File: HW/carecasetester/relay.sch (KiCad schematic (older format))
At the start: 1 part

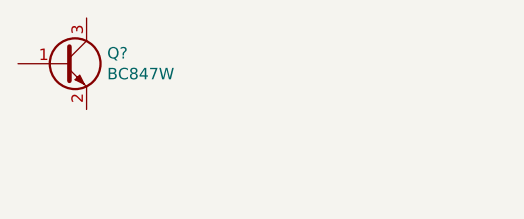
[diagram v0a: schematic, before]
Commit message: Main sheet saved still need to make relay sheet again
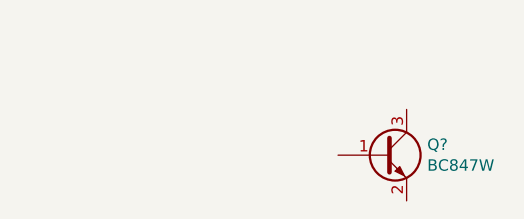
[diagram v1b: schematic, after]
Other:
- moved on the sheet: Q?
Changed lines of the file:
@@
 L Transistor_BJT:BC847W Q?
 U 1 1 5E853643
-P 3875 3400
-F 0 "Q?" H 4065 3446 50  0000 L CNN
-F 1 "BC847W" H 4065 3355 50  0000 L CNN
-F 2 "Package_TO_SOT_SMD:SOT-323_SC-70" H 4075 3325 50  0001 L CIN
-F 3 "http://www.infineon.com/dgdl/Infineon-BC847SERIES_BC848SERIES_BC849SERIES_BC850SERIES-DS-v01_01-en.pdf?fileId=db3a304314dca389011541d4630a1657" H 3875 3400 50  0001 L CNN
-	1    3875 3400
+P 5275 3800
+F 0 "Q?" H 5465 3846 50  0000 L CNN
+F 1 "BC847W" H 5465 3755 50  0000 L CNN
+F 2 "Package_TO_SOT_SMD:SOT-323_SC-70" H 5475 3725 50  0001 L CIN
+F 3 "http://www.infineon.com/dgdl/Infineon-BC847SERIES_BC848SERIES_BC849SERIES_BC850SERIES-DS-v01_01-en.pdf?fileId=db3a304314dca389011541d4630a1657" H 5275 3800 50  0001 L CNN
+	1    5275 3800
 	1    0    0    -1
 $EndComp

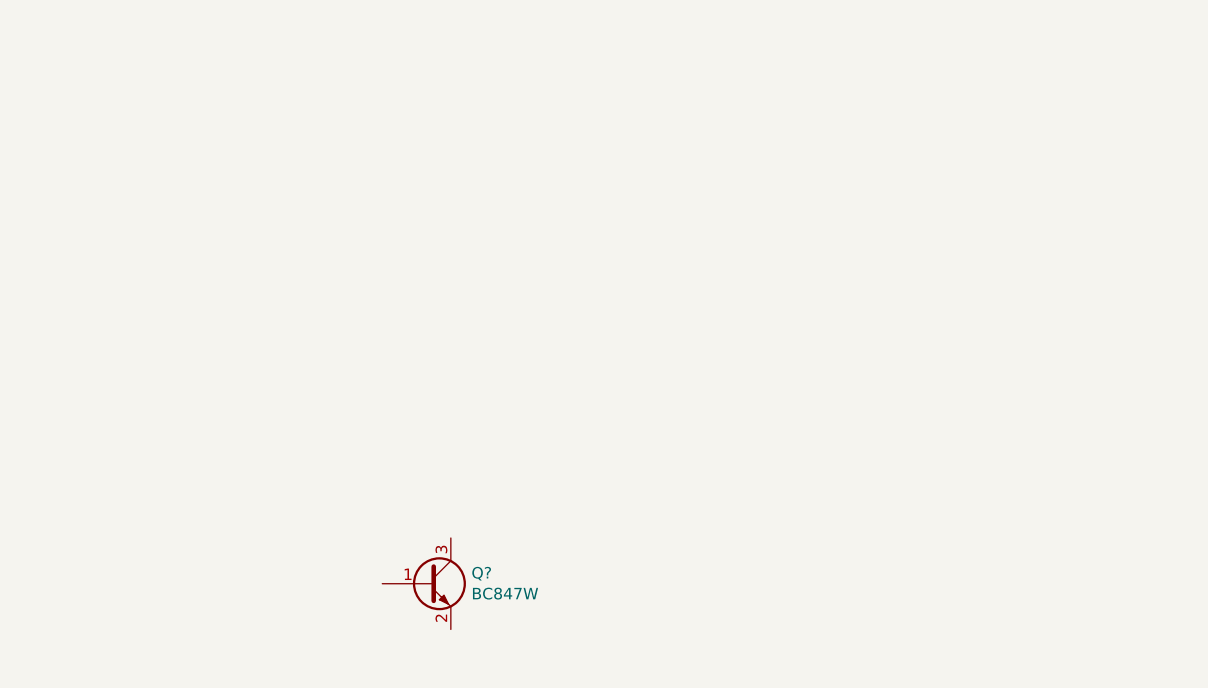
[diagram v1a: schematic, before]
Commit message: Relay sheet filled and all pins matched.
starting changes made to pcb to fit schematic to the new pcb
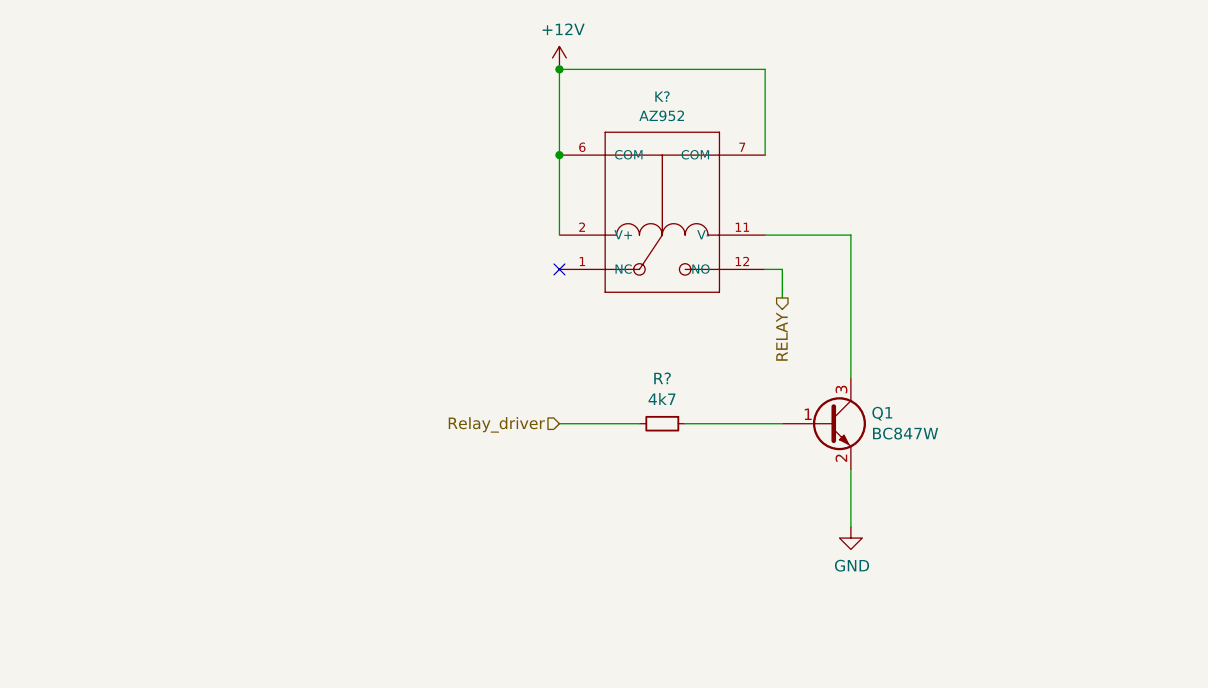
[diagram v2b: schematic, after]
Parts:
- added K?: AZ952, symbol athir:AZ952
- added R?: 4k7, symbol Device:R_Small
- gave numbers to parts that had none: 1
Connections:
- net at Q1.1 (B): now also R?.1
- net GND: now reaches Q1.2 (E)
- net at Q1.3 (C): now also K?.11 (V-)
- new net +12V: K?.2 (V+), K?.6 (COM), K?.7 (COM)
- new net RELAY: K?.12 (NO)
- new net Relay_driver: R?.2
- no-connect marks 0 -> 1
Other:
- moved on the sheet: Q1
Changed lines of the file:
@@
 $EndDescr
 $Comp
-L Transistor_BJT:BC847W Q?
+L Transistor_BJT:BC847W Q1
 U 1 1 5E853643
-P 5275 3800
-F 0 "Q?" H 5465 3846 50  0000 L CNN
-F 1 "BC847W" H 5465 3755 50  0000 L CNN
-F 2 "Package_TO_SOT_SMD:SOT-323_SC-70" H 5475 3725 50  0001 L CIN
-F 3 "http://www.infineon.com/dgdl/Infineon-BC847SERIES_BC848SERIES_BC849SERIES_BC850SERIES-DS-v01_01-en.pdf?fileId=db3a304314dca389011541d4630a1657" H 5275 3800 50  0001 L CNN
-	1    5275 3800
+P 7025 3100
+F 0 "Q1" H 7215 3146 50  0000 L CNN
+F 1 "BC847W" H 7215 3055 50  0000 L CNN
+F 2 "Package_TO_SOT_SMD:SOT-323_SC-70" H 7225 3025 50  0001 L CIN
+F 3 "http://www.infineon.com/dgdl/Infineon-BC847SERIES_BC848SERIES_BC849SERIES_BC850SERIES-DS-v01_01-en.pdf?fileId=db3a304314dca389011541d4630a1657" H 7025 3100 50  0001 L CNN
+	1    7025 3100
 	1    0    0    -1
 $EndComp
+$Comp
+L athir:AZ952 K?
+U 1 1 5E85B068
+P 6300 2175
+F 0 "K?" V 6804 2175 45  0000 C CNN
+F 1 "AZ952" V 6720 2175 45  0000 C CNN
+F 2 "" H 6300 2125 60  0001 C CNN
+F 3 "" H 6300 2125 60  0001 C CNN
+F 4 "315030000" H 6330 2275 20  0001 C CNN "SKU"
+	1    6300 2175
+	0    -1   -1   0
+$EndComp
+NoConn ~ 5850 2425
+Wire Wire Line
+	6750 1925 6750 1550
+Wire Wire Line
+	6750 1550 5850 1550
+Wire Wire Line
+	5850 1550 5850 1925
+Wire Wire Line
+	5850 2275 5850 1925
+Connection ~ 5850 1925
+$Comp
+L power:+12V #PWR?
+U 1 1 5E85C22D
+P 5850 1550
+F 0 "#PWR?" H 5850 1400 50  0001 C CNN
+F 1 "+12V" H 5865 1723 50  0000 C CNN
+F 2 "" H 5850 1550 50  0001 C CNN
+F 3 "" H 5850 1550 50  0001 C CNN
+	1    5850 1550
+	1    0    0    -1
+$EndComp
+Connection ~ 5850 1550
+Wire Wire Line
+	6750 2275 7125 2275
+Wire Wire Line
+	7125 2275 7125 2900
+$Comp
+L power:GND #PWR?
+U 1 1 5E85E92E
+P 7125 3550
+F 0 "#PWR?" H 7125 3300 50  0001 C CNN
+F 1 "GND" H 7130 3377 50  0000 C CNN
+F 2 "" H 7125 3550 50  0001 C CNN
+F 3 "" H 7125 3550 50  0001 C CNN
+	1    7125 3550
+	1    0    0    -1
+$EndComp
+Wire Wire Line
+	7125 3300 7125 3550
+$Comp
+L Device:R_Small R?
+U 1 1 5E85EFB5
+P 6300 3100
+F 0 "R?" V 6104 3100 50  0000 C CNN
+F 1 "4k7" V 6195 3100 50  0000 C CNN
+F 2 "" H 6300 3100 50  0001 C CNN
+F 3 "~" H 6300 3100 50  0001 C CNN
+	1    6300 3100
+	0    1    1    0
+$EndComp
+Wire Wire Line
+	6400 3100 6825 3100
+Text HLabel 5850 3100 0    50   Input ~ 0
+Relay_driver
+Wire Wire Line
+	5850 3100 6200 3100
+Text HLabel 6825 2550 3    50   Output ~ 0
+RELAY
+Wire Wire Line
+	6750 2425 6825 2425
+Wire Wire Line
+	6825 2425 6825 2550
 $EndSCHEMATC

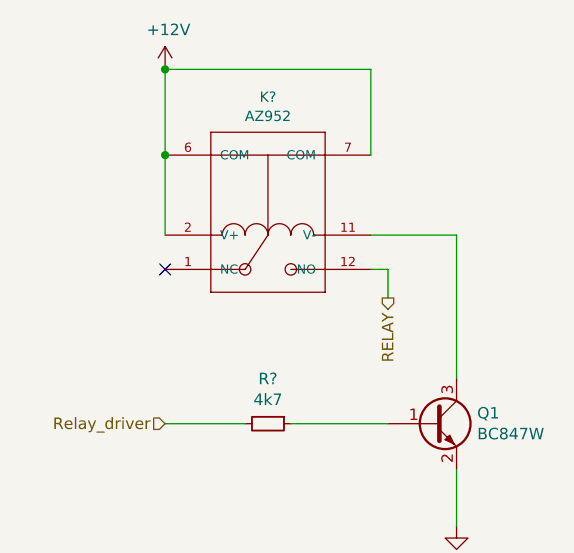
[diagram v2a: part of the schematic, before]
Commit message: First try to fit schematic to pcb (not imported footprints to pcb yet)
Schematic: All known components has gotten an updated footprint
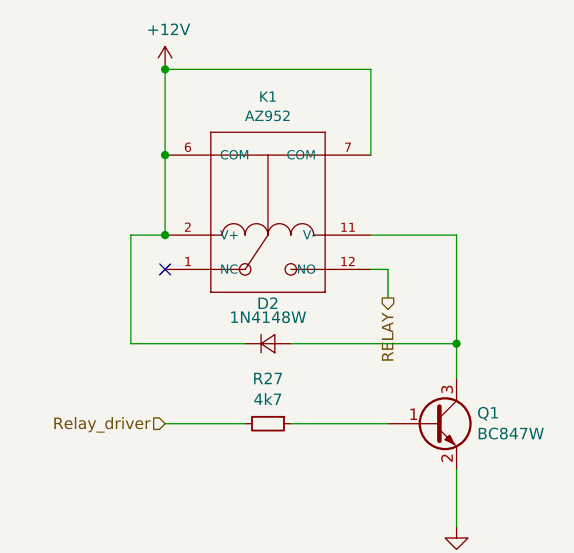
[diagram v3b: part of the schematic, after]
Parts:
- added D2: 1N4148W, Diode_THT:D_DO-35_SOD27_P10.16mm_Horizontal, symbol Device:D_Small
- K1: renamed from K?; footprint (none) -> athir:AZ952
- R27: renamed from R?; footprint (none) -> Resistor_SMD:R_0603_1608Metric_Pad1.05x0.95mm_HandSolder
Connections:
- net +12V: now also D2.1 (K)
- net at K1.11 (V-), Q1.3 (C): now also D2.2 (A)
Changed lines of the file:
@@
 $EndComp
 $Comp
-L athir:AZ952 K?
+L athir:AZ952 K1
 U 1 1 5E85B068
 P 6300 2175
-F 0 "K?" V 6804 2175 45  0000 C CNN
+F 0 "K1" V 6804 2175 45  0000 C CNN
 F 1 "AZ952" V 6720 2175 45  0000 C CNN
-F 2 "" H 6300 2125 60  0001 C CNN
+F 2 "athir:AZ952" H 6300 2125 60  0001 C CNN
 F 3 "" H 6300 2125 60  0001 C CNN
 F 4 "315030000" H 6330 2275 20  0001 C CNN "SKU"
@@
 Connection ~ 5850 1925
 $Comp
-L power:+12V #PWR?
+L power:+12V #PWR01
 U 1 1 5E85C22D
 P 5850 1550
-F 0 "#PWR?" H 5850 1400 50  0001 C CNN
+F 0 "#PWR01" H 5850 1400 50  0001 C CNN
 F 1 "+12V" H 5865 1723 50  0000 C CNN
 F 2 "" H 5850 1550 50  0001 C CNN
@@
 	6750 2275 7125 2275
 Wire Wire Line
-	7125 2275 7125 2900
+	7125 2275 7125 2750
 $Comp
-L power:GND #PWR?
+L power:GND #PWR06
 U 1 1 5E85E92E
 P 7125 3550
-F 0 "#PWR?" H 7125 3300 50  0001 C CNN
+F 0 "#PWR06" H 7125 3300 50  0001 C CNN
 F 1 "GND" H 7130 3377 50  0000 C CNN
 F 2 "" H 7125 3550 50  0001 C CNN
@@
 	7125 3300 7125 3550
 $Comp
-L Device:R_Small R?
+L Device:R_Small R27
 U 1 1 5E85EFB5
 P 6300 3100
-F 0 "R?" V 6104 3100 50  0000 C CNN
+F 0 "R27" V 6104 3100 50  0000 C CNN
 F 1 "4k7" V 6195 3100 50  0000 C CNN
-F 2 "" H 6300 3100 50  0001 C CNN
+F 2 "Resistor_SMD:R_0603_1608Metric_Pad1.05x0.95mm_HandSolder" H 6300 3100 50  0001 C CNN
 F 3 "~" H 6300 3100 50  0001 C CNN
 	1    6300 3100
@@
 Wire Wire Line
 	6825 2425 6825 2550
+$Comp
+L Device:D_Small D2
+U 1 1 5E867CA9
+P 6300 2750
+F 0 "D2" H 6300 2925 50  0000 C CNN
+F 1 "1N4148W" H 6300 2864 50  0000 C CNN
+F 2 "Diode_THT:D_DO-35_SOD27_P10.16mm_Horizontal" V 6300 2750 50  0001 C CNN
+F 3 "~" V 6300 2750 50  0001 C CNN
+	1    6300 2750
+	1    0    0    -1
+$EndComp
+Wire Wire Line
+	6200 2750 5700 2750
+Wire Wire Line
+	5700 2750 5700 2275
+Wire Wire Line
+	5700 2275 5850 2275
+Connection ~ 5850 2275
+Wire Wire Line
+	6400 2750 7125 2750
+Connection ~ 7125 2750
+Wire Wire Line
+	7125 2750 7125 2900
 $EndSCHEMATC

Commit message: PCB and Schematic are synced and gerbers can be made
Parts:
- Q1: footprint Package_TO_SOT_SMD:SOT-323_SC-70 -> Package_TO_SOT_SMD:SOT-23
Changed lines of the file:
@@
 F 0 "Q1" H 7215 3146 50  0000 L CNN
 F 1 "BC847W" H 7215 3055 50  0000 L CNN
-F 2 "Package_TO_SOT_SMD:SOT-323_SC-70" H 7225 3025 50  0001 L CIN
+F 2 "Package_TO_SOT_SMD:SOT-23" H 7225 3025 50  0001 L CIN
 F 3 "http://www.infineon.com/dgdl/Infineon-BC847SERIES_BC848SERIES_BC849SERIES_BC850SERIES-DS-v01_01-en.pdf?fileId=db3a304314dca389011541d4630a1657" H 7025 3100 50  0001 L CNN
 	1    7025 3100

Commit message: V0.22 gerbers
2nd relay added and all should now be ready to order
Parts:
- added D3: 1N4148W, Diode_THT:D_DO-35_SOD27_P10.16mm_Horizontal, symbol Device:D_Small
- added K2: AZ952, athir:AZ952, symbol carecasetester-rescue:AZ952-athir
- added Q2: BC847W, Package_TO_SOT_SMD:SOT-23, symbol Transistor_BJT:BC847W
- added R29: 4k7, Resistor_SMD:R_0603_1608Metric_Pad1.05x0.95mm_HandSolder, symbol Device:R_Small
- K1: symbol athir:AZ952 -> carecasetester-rescue:AZ952-athir
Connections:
- net GND: now also Q2.2 (E)
- net RELAY renamed RELAY12V
- net Relay_driver renamed Relay_driver1
- new net: Q2.1 (B), R29.1
- new net: D3.2 (A), K2.11 (V-), Q2.3 (C)
- new net +5V: D3.1 (K), K2.2 (V+), K2.6 (COM), K2.7 (COM)
- new net RELAYBAT: K2.12 (NO)
- new net Relay_driver2: R29.2
- no-connect marks 1 -> 2
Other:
- moved on the sheet: D2, K1, Q1, R27
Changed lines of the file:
@@
 L Transistor_BJT:BC847W Q1
 U 1 1 5E853643
-P 7025 3100
-F 0 "Q1" H 7215 3146 50  0000 L CNN
-F 1 "BC847W" H 7215 3055 50  0000 L CNN
-F 2 "Package_TO_SOT_SMD:SOT-23" H 7225 3025 50  0001 L CIN
-F 3 "http://www.infineon.com/dgdl/Infineon-BC847SERIES_BC848SERIES_BC849SERIES_BC850SERIES-DS-v01_01-en.pdf?fileId=db3a304314dca389011541d4630a1657" H 7025 3100 50  0001 L CNN
-	1    7025 3100
-	1    0    0    -1
-$EndComp
-$Comp
-L athir:AZ952 K1
+P 5350 3475
+F 0 "Q1" H 5540 3521 50  0000 L CNN
+F 1 "BC847W" H 5540 3430 50  0000 L CNN
+F 2 "Package_TO_SOT_SMD:SOT-23" H 5550 3400 50  0001 L CIN
+F 3 "http://www.infineon.com/dgdl/Infineon-BC847SERIES_BC848SERIES_BC849SERIES_BC850SERIES-DS-v01_01-en.pdf?fileId=db3a304314dca389011541d4630a1657" H 5350 3475 50  0001 L CNN
+	1    5350 3475
+	1    0    0    -1
+$EndComp
+$Comp
+L carecasetester-rescue:AZ952-athir K1
 U 1 1 5E85B068
-P 6300 2175
-F 0 "K1" V 6804 2175 45  0000 C CNN
-F 1 "AZ952" V 6720 2175 45  0000 C CNN
-F 2 "athir:AZ952" H 6300 2125 60  0001 C CNN
-F 3 "" H 6300 2125 60  0001 C CNN
-F 4 "315030000" H 6330 2275 20  0001 C CNN "SKU"
-	1    6300 2175
+P 4625 2550
+AR Path="/5E85B068" Ref="K1"  Part="1"
+AR Path="/5E3E43C1/5E85B068" Ref="K1"  Part="1"
+F 0 "K1" V 5129 2550 45  0000 C CNN
+F 1 "AZ952" V 5045 2550 45  0000 C CNN
+F 2 "athir:AZ952" H 4625 2500 60  0001 C CNN
+F 3 "" H 4625 2500 60  0001 C CNN
+F 4 "315030000" H 4655 2650 20  0001 C CNN "SKU"
+	1    4625 2550
 	0    -1   -1   0
 $EndComp
-NoConn ~ 5850 2425
-Wire Wire Line
-	6750 1925 6750 1550
-Wire Wire Line
-	6750 1550 5850 1550
-Wire Wire Line
-	5850 1550 5850 1925
-Wire Wire Line
-	5850 2275 5850 1925
-Connection ~ 5850 1925
+NoConn ~ 4175 2800
+Wire Wire Line
+	5075 2300 5075 1925
+Wire Wire Line
+	5075 1925 4175 1925
+Wire Wire Line
+	4175 1925 4175 2300
+Wire Wire Line
+	4175 2650 4175 2300
+Connection ~ 4175 2300
 $Comp
 L power:+12V #PWR01
 U 1 1 5E85C22D
-P 5850 1550
-F 0 "#PWR01" H 5850 1400 50  0001 C CNN
-F 1 "+12V" H 5865 1723 50  0000 C CNN
-F 2 "" H 5850 1550 50  0001 C CNN
-F 3 "" H 5850 1550 50  0001 C CNN
-	1    5850 1550
-	1    0    0    -1
-$EndComp
-Connection ~ 5850 1550
-Wire Wire Line
-	6750 2275 7125 2275
-Wire Wire Line
-	7125 2275 7125 2750
+P 4175 1925
+F 0 "#PWR01" H 4175 1775 50  0001 C CNN
+F 1 "+12V" H 4190 2098 50  0000 C CNN
+F 2 "" H 4175 1925 50  0001 C CNN
+F 3 "" H 4175 1925 50  0001 C CNN
+	1    4175 1925
+	1    0    0    -1
+$EndComp
+Connection ~ 4175 1925
+Wire Wire Line
+	5075 2650 5450 2650
+Wire Wire Line
+	5450 2650 5450 3125
 $Comp
 L power:GND #PWR06
 U 1 1 5E85E92E
-P 7125 3550
-F 0 "#PWR06" H 7125 3300 50  0001 C CNN
-F 1 "GND" H 7130 3377 50  0000 C CNN
-F 2 "" H 7125 3550 50  0001 C CNN
-F 3 "" H 7125 3550 50  0001 C CNN
-	1    7125 3550
-	1    0    0    -1
-$EndComp
-Wire Wire Line
-	7125 3300 7125 3550
+P 5450 3925
+F 0 "#PWR06" H 5450 3675 50  0001 C CNN
+F 1 "GND" H 5455 3752 50  0000 C CNN
+F 2 "" H 5450 3925 50  0001 C CNN
+F 3 "" H 5450 3925 50  0001 C CNN
+	1    5450 3925
+	1    0    0    -1
+$EndComp
+Wire Wire Line
+	5450 3675 5450 3925
 $Comp
 L Device:R_Small R27
 U 1 1 5E85EFB5
-P 6300 3100
-F 0 "R27" V 6104 3100 50  0000 C CNN
-F 1 "4k7" V 6195 3100 50  0000 C CNN
-F 2 "Resistor_SMD:R_0603_1608Metric_Pad1.05x0.95mm_HandSolder" H 6300 3100 50  0001 C CNN
-F 3 "~" H 6300 3100 50  0001 C CNN
-	1    6300 3100
+P 4625 3475
+F 0 "R27" V 4429 3475 50  0000 C CNN
+F 1 "4k7" V 4520 3475 50  0000 C CNN
+F 2 "Resistor_SMD:R_0603_1608Metric_Pad1.05x0.95mm_HandSolder" H 4625 3475 50  0001 C CNN
+F 3 "~" H 4625 3475 50  0001 C CNN
+	1    4625 3475
 	0    1    1    0
 $EndComp
 Wire Wire Line
-	6400 3100 6825 3100
-Text HLabel 5850 3100 0    50   Input ~ 0
-Relay_driver
-Wire Wire Line
-	5850 3100 6200 3100
-Text HLabel 6825 2550 3    50   Output ~ 0
-RELAY
-Wire Wire Line
-	6750 2425 6825 2425
-Wire Wire Line
-	6825 2425 6825 2550
+	4725 3475 5150 3475
+Text HLabel 4175 3475 0    50   Input ~ 0
+Relay_driver1
+Wire Wire Line
+	4175 3475 4525 3475
+Text HLabel 5150 2925 3    50   Output ~ 0
+RELAY12V
+Wire Wire Line
+	5075 2800 5150 2800
+Wire Wire Line
+	5150 2800 5150 2925
 $Comp
 L Device:D_Small D2
 U 1 1 5E867CA9
-P 6300 2750
-F 0 "D2" H 6300 2925 50  0000 C CNN
-F 1 "1N4148W" H 6300 2864 50  0000 C CNN
-F 2 "Diode_THT:D_DO-35_SOD27_P10.16mm_Horizontal" V 6300 2750 50  0001 C CNN
-F 3 "~" V 6300 2750 50  0001 C CNN
-	1    6300 2750
-	1    0    0    -1
-$EndComp
-Wire Wire Line
-	6200 2750 5700 2750
-Wire Wire Line
-	5700 2750 5700 2275
-Wire Wire Line
-	5700 2275 5850 2275
-Connection ~ 5850 2275
-Wire Wire Line
-	6400 2750 7125 2750
-Connection ~ 7125 2750
-Wire Wire Line
-	7125 2750 7125 2900
+P 4625 3125
+F 0 "D2" H 4625 3300 50  0000 C CNN
+F 1 "1N4148W" H 4625 3239 50  0000 C CNN
+F 2 "Diode_THT:D_DO-35_SOD27_P10.16mm_Horizontal" V 4625 3125 50  0001 C CNN
+F 3 "~" V 4625 3125 50  0001 C CNN
+	1    4625 3125
+	1    0    0    -1
+$EndComp
+Wire Wire Line
+	4525 3125 4025 3125
+Wire Wire Line
+	4025 3125 4025 2650
+Wire Wire Line
+	4025 2650 4175 2650
+Connection ~ 4175 2650
+Wire Wire Line
+	4725 3125 5450 3125
+Connection ~ 5450 3125
+Wire Wire Line
+	5450 3125 5450 3275
+$Comp
+L Transistor_BJT:BC847W Q2
+U 1 1 5E8BC0FC
+P 8075 3500
+F 0 "Q2" H 8265 3546 50  0000 L CNN
+F 1 "BC847W" H 8265 3455 50  0000 L CNN
+F 2 "Package_TO_SOT_SMD:SOT-23" H 8275 3425 50  0001 L CIN
+F 3 "http://www.infineon.com/dgdl/Infineon-BC847SERIES_BC848SERIES_BC849SERIES_BC850SERIES-DS-v01_01-en.pdf?fileId=db3a304314dca389011541d4630a1657" H 8075 3500 50  0001 L CNN
+	1    8075 3500
+	1    0    0    -1
+$EndComp
+$Comp
+L carecasetester-rescue:AZ952-athir K?
+U 1 1 5E8BC103
+P 7350 2575
+AR Path="/5E8BC103" Ref="K?"  Part="1"
+AR Path="/5E3E43C1/5E8BC103" Ref="K2"  Part="1"
+F 0 "K2" V 7854 2575 45  0000 C CNN
+F 1 "AZ952" V 7770 2575 45  0000 C CNN
+F 2 "athir:AZ952" H 7350 2525 60  0001 C CNN
+F 3 "" H 7350 2525 60  0001 C CNN
+F 4 "315030000" H 7380 2675 20  0001 C CNN "SKU"
+	1    7350 2575
+	0    -1   -1   0
+$EndComp
+NoConn ~ 6900 2825
+Wire Wire Line
+	7800 2325 7800 1950
+Wire Wire Line
+	7800 1950 6900 1950
+Wire Wire Line
+	6900 1950 6900 2325
+Wire Wire Line
+	6900 2675 6900 2325
+Connection ~ 6900 2325
+Wire Wire Line
+	7800 2675 8175 2675
+Wire Wire Line
+	8175 2675 8175 3150
+$Comp
+L power:GND #PWR09
+U 1 1 5E8BC118
+P 8175 3950
+F 0 "#PWR09" H 8175 3700 50  0001 C CNN
+F 1 "GND" H 8180 3777 50  0000 C CNN
+F 2 "" H 8175 3950 50  0001 C CNN
+F 3 "" H 8175 3950 50  0001 C CNN
+	1    8175 3950
+	1    0    0    -1
+$EndComp
+Wire Wire Line
+	8175 3700 8175 3950
+$Comp
+L Device:R_Small R29
+U 1 1 5E8BC11F
+P 7350 3500
+F 0 "R29" V 7154 3500 50  0000 C CNN
+F 1 "4k7" V 7245 3500 50  0000 C CNN
+F 2 "Resistor_SMD:R_0603_1608Metric_Pad1.05x0.95mm_HandSolder" H 7350 3500 50  0001 C CNN
+F 3 "~" H 7350 3500 50  0001 C CNN
+	1    7350 3500
+	0    1    1    0
+$EndComp
+Wire Wire Line
+	7450 3500 7875 3500
+Text HLabel 6900 3500 0    50   Input ~ 0
+Relay_driver2
+Wire Wire Line
+	6900 3500 7250 3500
+Text HLabel 7875 2950 3    50   Output ~ 0
+RELAYBAT
+Wire Wire Line
+	7800 2825 7875 2825
+Wire Wire Line
+	7875 2825 7875 2950
+$Comp
+L Device:D_Small D3
+U 1 1 5E8BC12B
+P 7350 3150
+F 0 "D3" H 7350 3325 50  0000 C CNN
+F 1 "1N4148W" H 7350 3264 50  0000 C CNN
+F 2 "Diode_THT:D_DO-35_SOD27_P10.16mm_Horizontal" V 7350 3150 50  0001 C CNN
+F 3 "~" V 7350 3150 50  0001 C CNN
+	1    7350 3150
+	1    0    0    -1
+$EndComp
+Wire Wire Line
+	7250 3150 6750 3150
+Wire Wire Line
+	6750 3150 6750 2675
+Wire Wire Line
+	6750 2675 6900 2675
+Connection ~ 6900 2675
+Wire Wire Line
+	7450 3150 8175 3150
+Connection ~ 8175 3150
+Wire Wire Line
+	8175 3150 8175 3300
+$Comp
+L power:+5V #PWR?
+U 1 1 5E8CEDFA
+P 6900 1950
+F 0 "#PWR?" H 6900 1800 50  0001 C CNN
+F 1 "+5V" H 6915 2123 50  0000 C CNN
+F 2 "" H 6900 1950 50  0001 C CNN
+F 3 "" H 6900 1950 50  0001 C CNN
+	1    6900 1950
+	1    0    0    -1
+$EndComp
+Connection ~ 6900 1950
 $EndSCHEMATC
